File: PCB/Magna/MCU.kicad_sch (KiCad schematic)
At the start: 51 parts, among them J201 Conn_02x06_Odd_Even, J202 Conn_ARM_JTAG_SWD_20, J203 Boot Jumper, U201 STM32F730V8T6, U202 24.576 MHz, Y201 24MHz

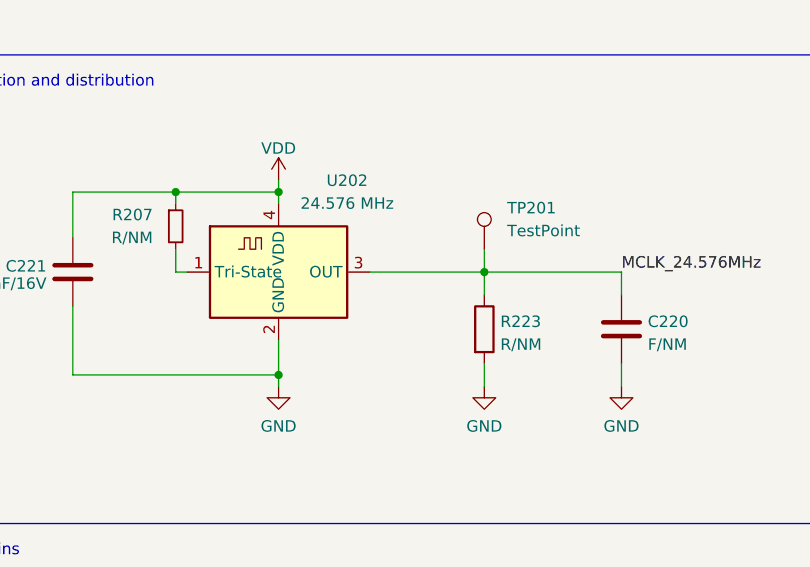
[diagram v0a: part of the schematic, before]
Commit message: Update some files to KiCad8 and make ready for production
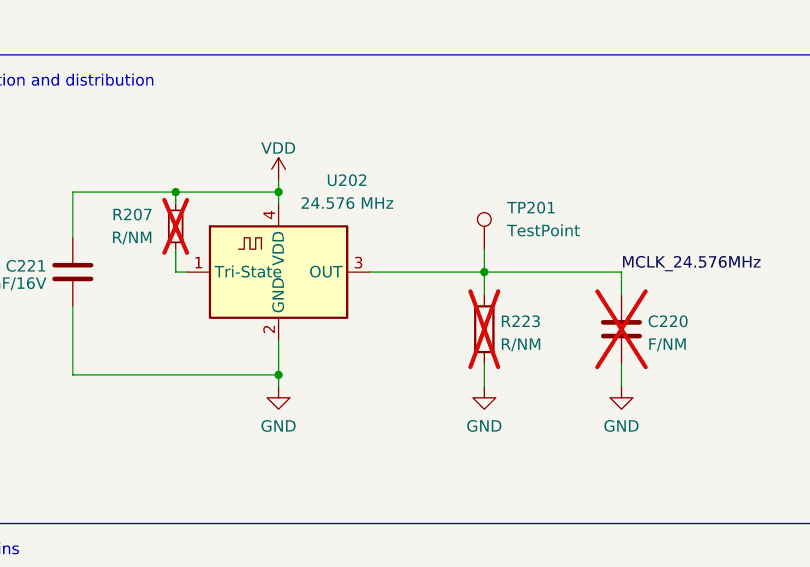
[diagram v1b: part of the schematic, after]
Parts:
- C220, R207, R223: now not fitted; now left out of the parts list

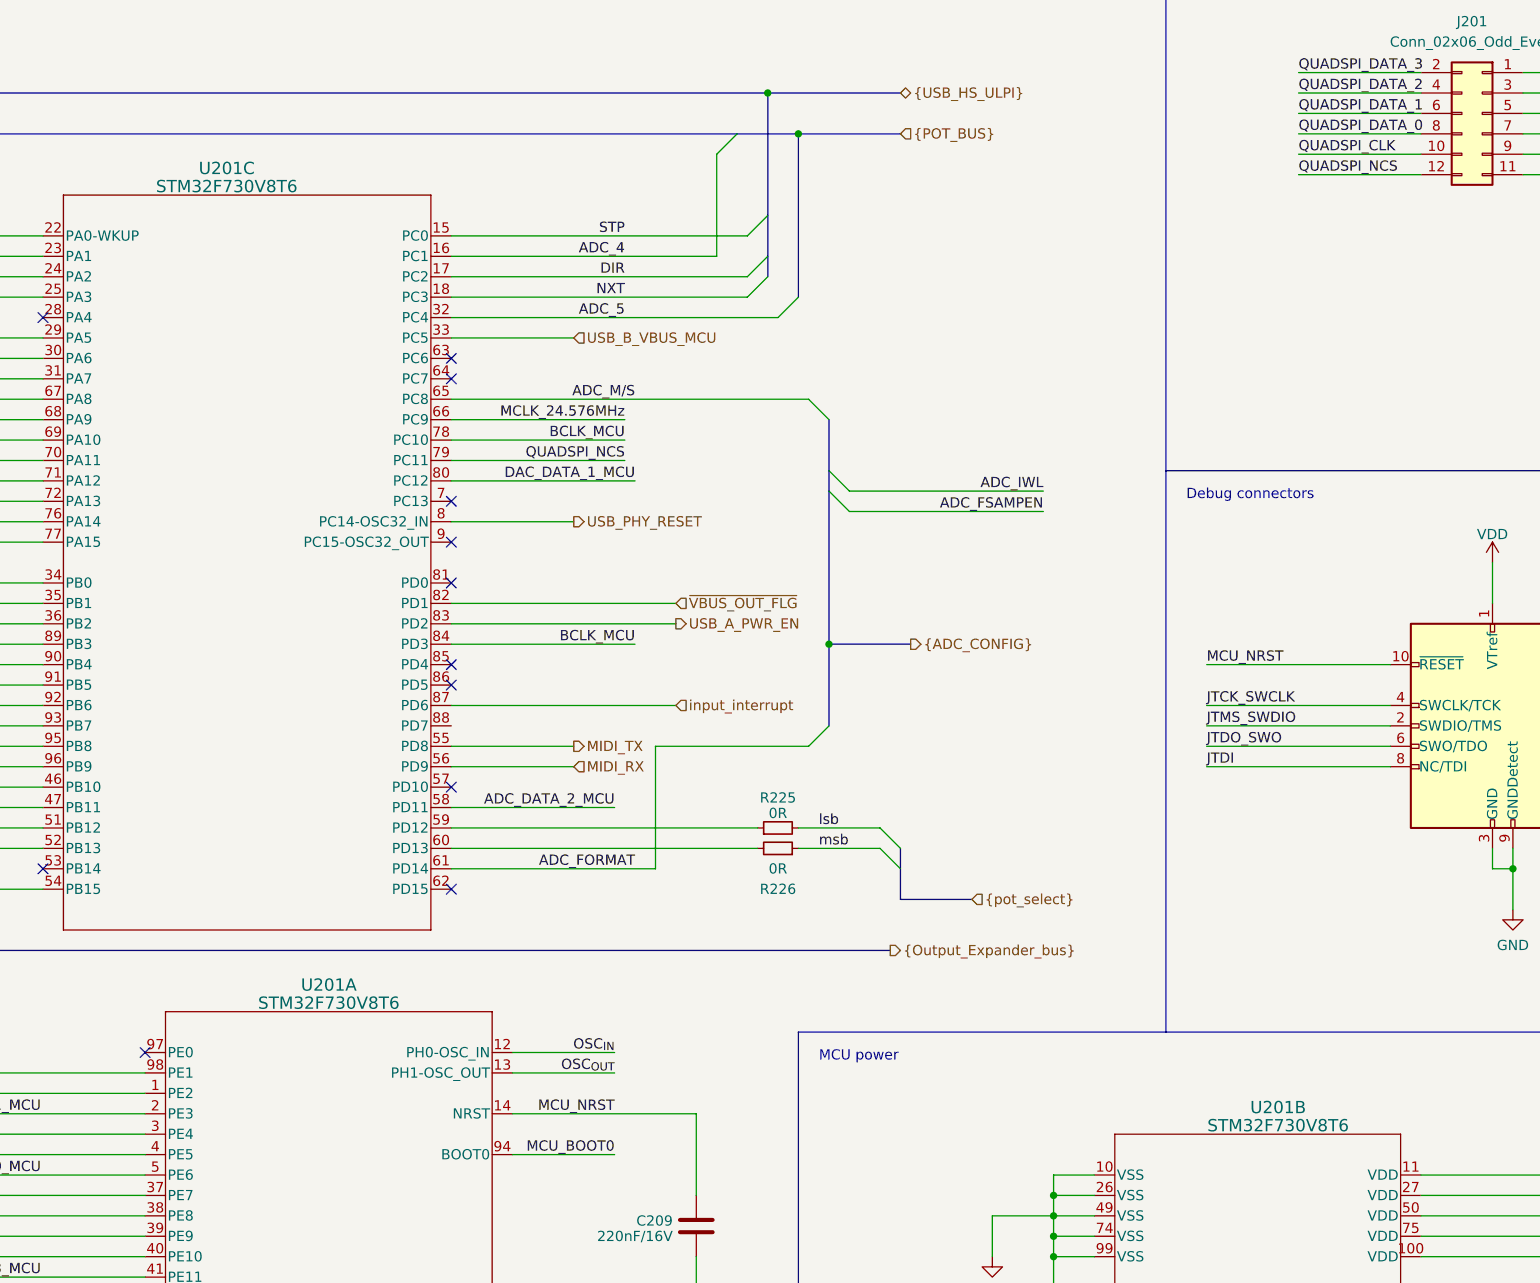
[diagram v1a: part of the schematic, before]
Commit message: Update Project to Kicad 8.0 and prepare for production
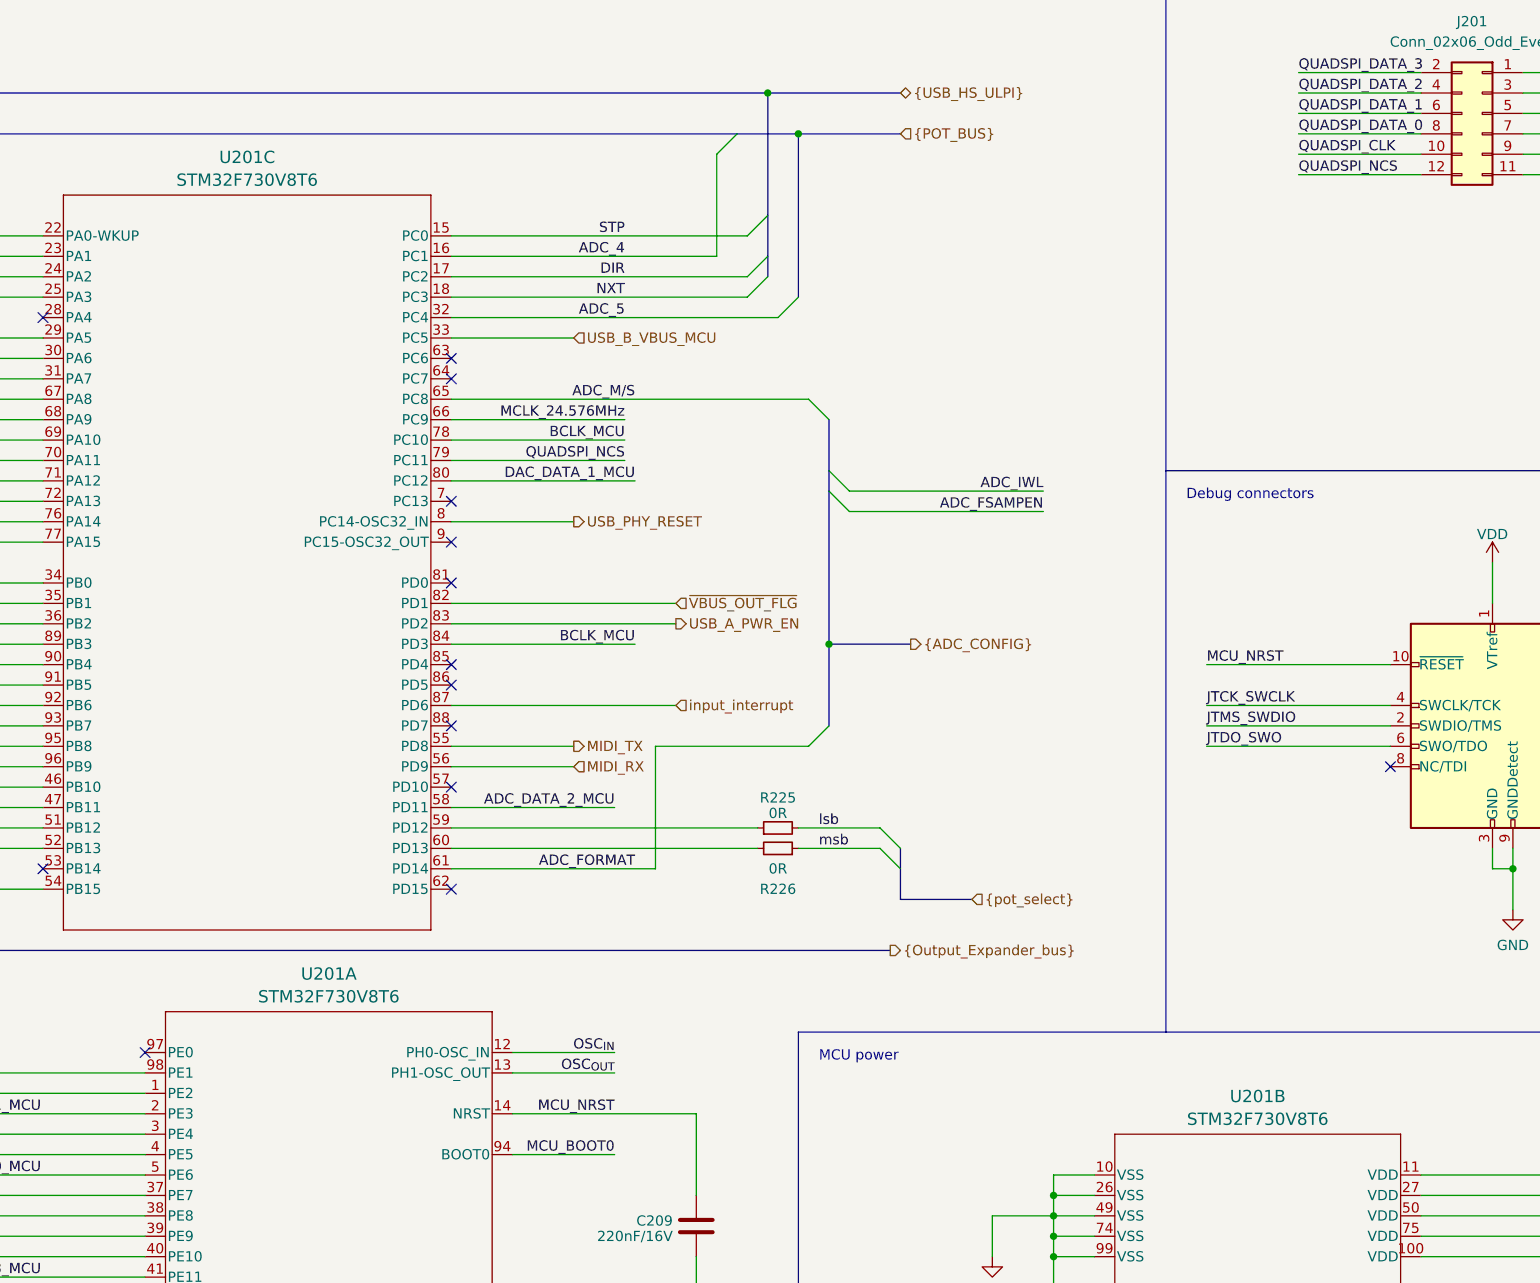
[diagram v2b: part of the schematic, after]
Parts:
- U201: symbol Skrooter_symbols:STM32F730V8T6 -> SkrooterLib:STM32F730V8T6
- U202: footprint Oscillator:Oscillator_SMD_Abracon_ASE-4Pin_3.2x2.5mm_HandSoldering -> Crystal:Crystal_SMD_3225-4Pin_3.2x2.5mm
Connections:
- net JTDI: no longer names the net of J202.8 (NC/TDI)
- no-connect marks 12 -> 14

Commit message: Some updates to PCB
Honestly I cannot remember whats changed
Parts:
- J201, J202, J203: now left out of the parts list
- R206: LCSC C2686517 -> C17714
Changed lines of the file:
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@@
 			)
 		)
-		(property "LCSC" "C2686517"
+		(property "LCSC" "C17714"
 			(at 256.54 248.92 90)
 			(effects
@@
 		(unit 1)
 		(exclude_from_sim no)
-		(in_bom yes)
+		(in_bom no)
 		(on_board yes)
 		(dnp no)
@@
 		(unit 1)
 		(exclude_from_sim no)
-		(in_bom yes)
+		(in_bom no)
 		(on_board yes)
 		(dnp no)
@@
 		(unit 1)
 		(exclude_from_sim no)
-		(in_bom yes)
+		(in_bom no)
 		(on_board yes)
 		(dnp no)

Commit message: Update schematics to Kicad 9
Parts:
- U201: symbol SkrooterLib:STM32F730V8T6 -> Skrooter_symbols:STM32F730V8T6
- U202: footprint Crystal:Crystal_SMD_3225-4Pin_3.2x2.5mm -> Oscillator:Oscillator_SMD_ECS_2520MV-xxx-xx-4Pin_2.5x2.0mm

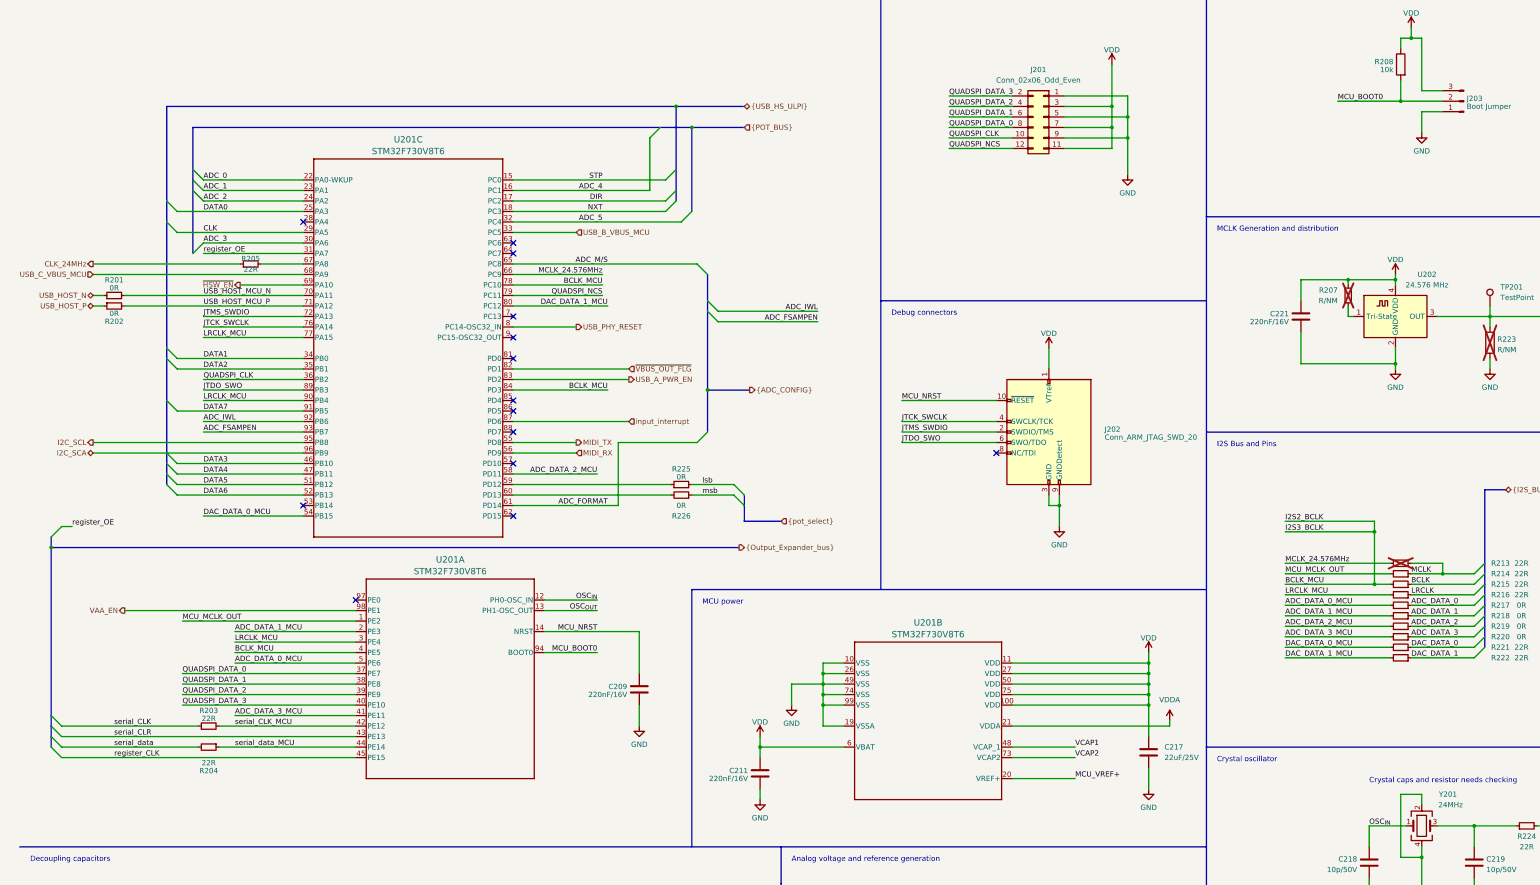
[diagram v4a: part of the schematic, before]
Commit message: Update Mainboard PCB
* Added better power ORing
* Added DRC for length matching
* Changed out components for cheaper production
* Removed some optional circuits from BOM for first prototype
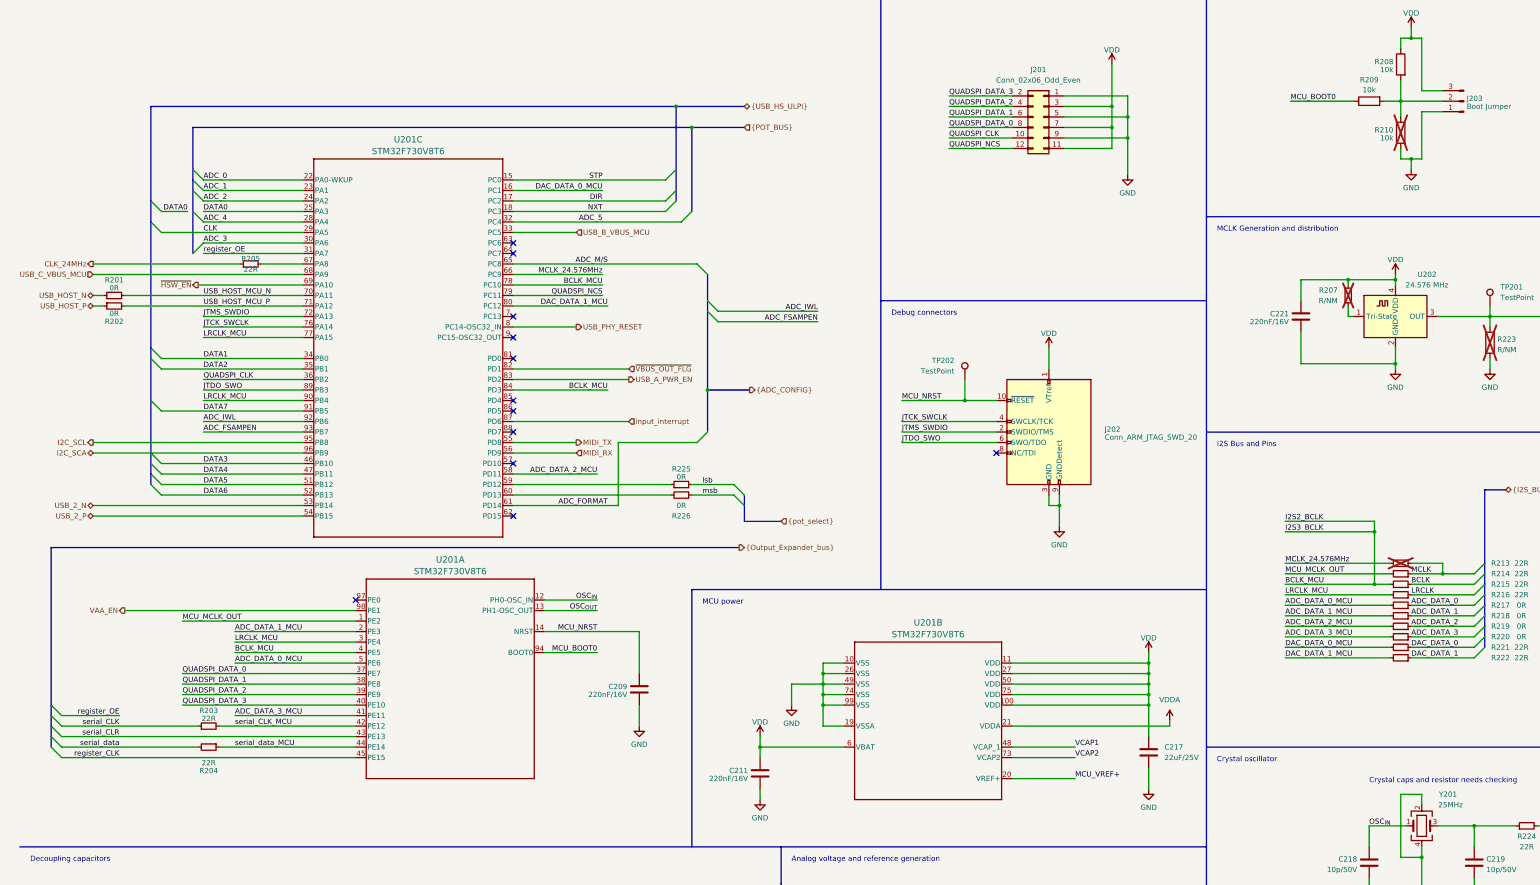
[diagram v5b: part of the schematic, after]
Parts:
- added R209, R210: 10k, Resistor_SMD:R_0805_2012Metric_Pad1.20x1.40mm_HandSolder, symbol Device:R
- added TP202: TestPoint, TestPoint:TestPoint_Keystone_5000-5004_Miniature, symbol Connector:TestPoint
- TP201: now left out of the parts list
- U201: LCSC C435845 -> C404010
- Y201: value 24MHz -> 25MHz; LCSC C648933 -> C9006
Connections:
- net ADC_4: now also U201.28 (PA4); no longer U201.16 (PC1)
- net DAC_DATA_0_MCU: now also U201.16 (PC1); no longer U201.54 (PB15)
- net GND: now also R210.2
- net MCU_BOOT0: now also R209.1; no longer J203.2 (Pin_2), R208.2
- net MCU_NRST: now also TP202.1
- net USB_2_N: now reaches U201.53 (PB14)
- new net: J203.2 (Pin_2), R208.2, R209.2, R210.1
- new net USB_2_P: U201.54 (PB15)
- no-connect marks 14 -> 12
